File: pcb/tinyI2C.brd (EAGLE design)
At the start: 84 x 83.2 mm, 37 parts, among them IC1 74LVC1G125DCK, IC2 74LVC1G125DCK, IC3 IC_LDO_MIC5355, U1 LPC824M201JHI33, X1 TSW-112-02-S-S, X2 TSW-112-02-S-S, X3 TSW-106-02-S-S-RA, X4 TSW-102-02-S-S, X5 TSW-102-02-S-S, X6 TSW-102-02-S-S

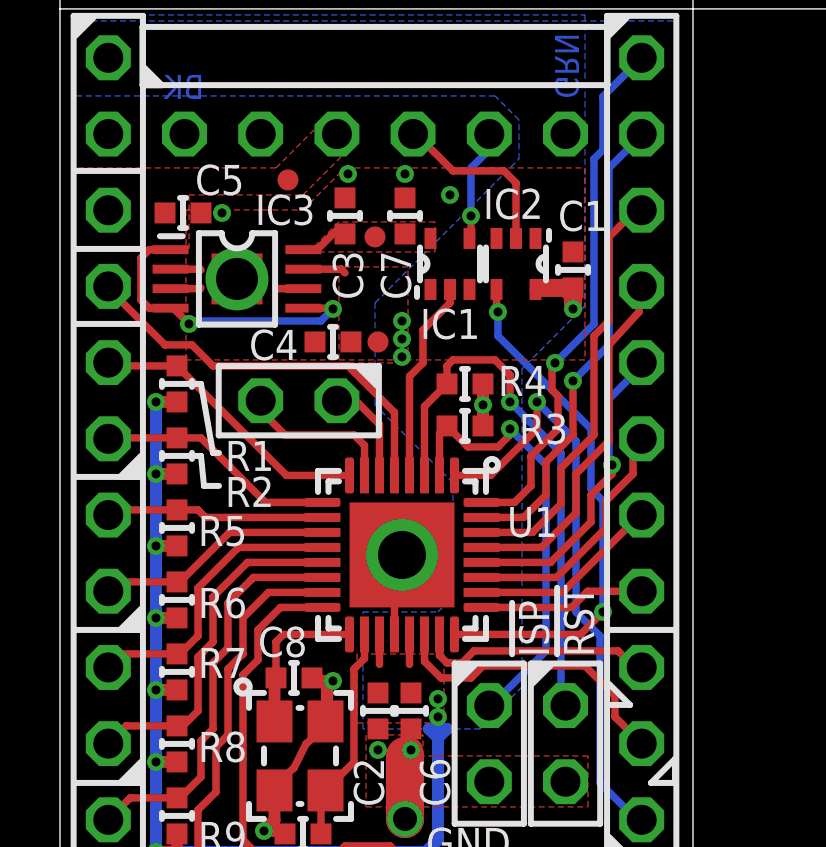
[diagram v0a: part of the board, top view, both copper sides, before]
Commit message: [ PCB ][ BRD ] silk/library update
Silk: pin 1 indicator added (x3)
Library: mylib; IC_LDO_MIC5355; related trace change
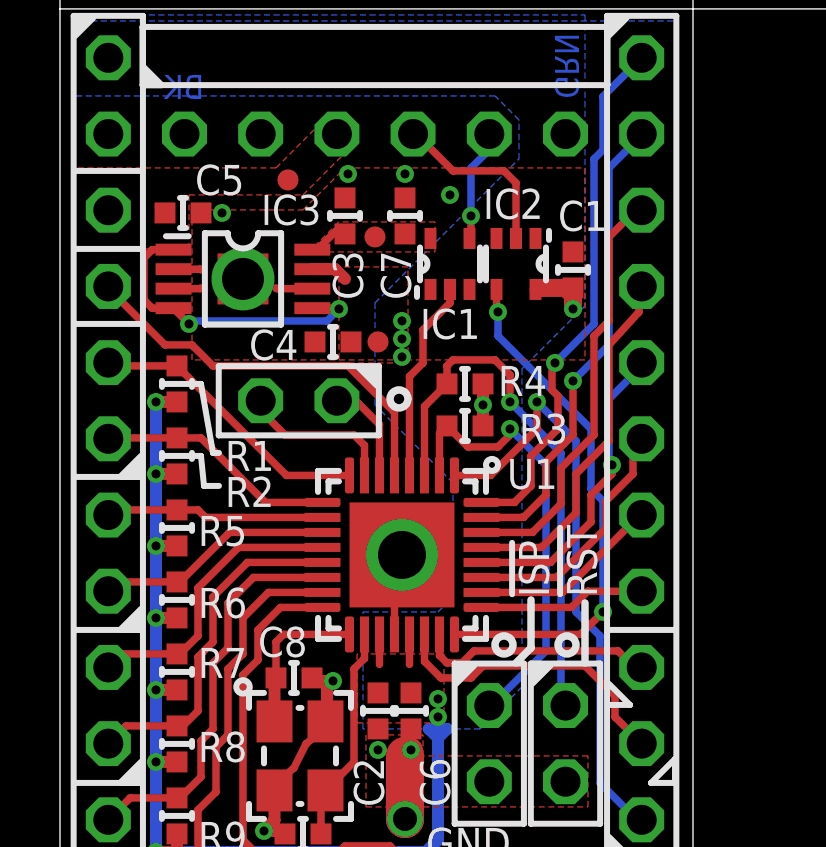
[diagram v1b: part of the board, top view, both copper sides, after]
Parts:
- moved IC3 0.20 mm to (6.10, 32.6)
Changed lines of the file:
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@@
 <grid distance="0.1" unitdist="mm" unit="mm" style="dots" multiple="1" display="yes" altdistance="0.05" altunitdist="mm" altunit="mm"/>
 <layers>
-<layer number="1" name="Top" color="12" fill="1" visible="yes" active="yes"/>
+<layer number="1" name="Top" color="12" fill="0" visible="yes" active="yes"/>
 <layer number="16" name="Bottom" color="1" fill="1" visible="yes" active="yes"/>
 <layer number="17" name="Pads" color="2" fill="1" visible="yes" active="yes"/>
@@
 <wire x1="13.4" y1="32.6" x2="13.4" y2="31.9" width="0.1" layer="41"/>
 <wire x1="13.9" y1="31.9" x2="13.9" y2="32.6" width="0.1" layer="41"/>
-<text x="17.8" y="20" size="1" layer="21" font="vector" ratio="20" rot="R90">!RST</text>
-<text x="16.3" y="20" size="1" layer="21" font="vector" ratio="20" rot="R90">!ISP</text>
+<text x="17.9" y="22" size="1" layer="21" font="vector" ratio="20" rot="R90">!RST</text>
+<text x="16.3" y="22" size="1" layer="21" font="vector" ratio="20" rot="R90">!ISP</text>
 <wire x1="9" y1="30" x2="9" y2="31" width="0.2" layer="41"/>
 <wire x1="9" y1="30" x2="8.2" y2="30" width="0.2" layer="41"/>
@@
 <wire x1="4.7" y1="29.1" x2="5.1" y2="26.8" width="0.2" layer="21"/>
 <wire x1="4.7" y1="26.7" x2="4.8" y2="25.7" width="0.2" layer="21"/>
-<wire x1="11.6" y1="31.7" x2="11.2" y2="31.7" width="0.1" layer="41"/>
-<wire x1="10.6" y1="31.1" x2="11.2" y2="31.7" width="0.1" layer="41" curve="-90"/>
-<wire x1="10.6" y1="33" x2="10.6" y2="31.1" width="0.1" layer="41"/>
+<wire x1="11.6" y1="31.7" x2="11.4" y2="31.7" width="0.1" layer="41"/>
+<wire x1="10.8" y1="31.1" x2="11.4" y2="31.7" width="0.1" layer="41" curve="-90"/>
+<wire x1="10.8" y1="33" x2="10.8" y2="31.1" width="0.1" layer="41"/>
 <wire x1="12.1" y1="31.8" x2="12.1" y2="32.6" width="0.1" layer="41"/>
 <wire x1="12.6" y1="31.8" x2="12.1" y2="31.8" width="0.2" layer="41"/>
@@
 <wire x1="20.5" y1="15.8" x2="20.5" y2="16.6" width="0.2" layer="21"/>
 <wire x1="20.5" y1="16.6" x2="19.7" y2="15.8" width="0.2" layer="21"/>
-<wire x1="7.6" y1="32.5" x2="8.7" y2="32.5" width="0.2" layer="41"/>
-<wire x1="7.6" y1="32" x2="8.7" y2="32" width="0.2" layer="41"/>
-<wire x1="8.7" y1="32" x2="8.7" y2="32.5" width="0.2" layer="41"/>
-<wire x1="4.2" y1="32.5" x2="3.7" y2="32.5" width="0.2" layer="41"/>
-<wire x1="4.2" y1="32" x2="3.7" y2="32" width="0.2" layer="41"/>
+<wire x1="7.9" y1="32.5" x2="9" y2="32.5" width="0.2" layer="41"/>
+<wire x1="7.9" y1="32" x2="9" y2="32" width="0.2" layer="41"/>
+<wire x1="9" y1="32" x2="9" y2="32.5" width="0.2" layer="41"/>
+<wire x1="4.1" y1="32.5" x2="3.6" y2="32.5" width="0.2" layer="41"/>
+<wire x1="4.1" y1="32" x2="3.6" y2="32" width="0.2" layer="41"/>
 <polygon width="0.2" layer="30">
 <vertex x="5.9" y="33.5" curve="-90"/>
@@
 <wire x1="14.2" y1="31.9" x2="13.9" y2="31.9" width="0.1" layer="41"/>
 <wire x1="14.2" y1="32.6" x2="13.9" y2="32.6" width="0.1" layer="41"/>
+<circle x="11.3" y="28.6" radius="0.3" width="0.25" layer="21"/>
+<circle x="14.8" y="20.4" radius="0.3" width="0.25" layer="21"/>
+<circle x="16.9" y="20.4" radius="0.3" width="0.25" layer="21"/>
+<wire x1="15.7" y1="21.9" x2="15.7" y2="20.3" width="0.25" layer="21"/>
+<wire x1="15.7" y1="20.3" x2="15.2" y2="19.8" width="0.25" layer="21"/>
+<wire x1="17.5" y1="21.8" x2="17.5" y2="19.8" width="0.25" layer="21"/>
 </plain>
 <attributes>
@@
 </element>
 <element name="U1" library="mylib" package="HVQFN33" value="LPC824M201JHI33" x="11.4" y="23.4" smashed="yes" rot="R270">
-<attribute name="NAME" x="14.9" y="24" size="1" layer="25" font="vector" ratio="20"/>
+<attribute name="NAME" x="14.9" y="25.6" size="1" layer="25" font="vector" ratio="20"/>
 <attribute name="VALUE" x="6.9" y="25.9" size="1.27" layer="27" ratio="10" rot="R270"/>
 </element>
@@
 <attribute name="VALUE" x="13.405" y="34.065" size="1.27" layer="27" rot="R90"/>
 </element>
-<element name="IC3" library="mylib" package="IC_08_0.65_160MIL" value="IC_LDO_MIC5355" x="5.9" y="32.6" smashed="yes" rot="R270">
-<attribute name="NAME" x="6.5" y="34.4" size="1" layer="25" font="vector" ratio="20"/>
-<attribute name="VALUE" x="3.36" y="29.298" size="1.27" layer="27" ratio="10"/>
+<element name="IC3" library="mylib" package="IC_08_0.65_160MIL" value="IC_LDO_MIC5355" x="6.1" y="32.6" smashed="yes" rot="R270">
+<attribute name="NAME" x="6.7" y="34.4" size="1" layer="25" font="vector" ratio="20"/>
+<attribute name="VALUE" x="3.56" y="29.298" size="1.27" layer="27" ratio="10"/>
 </element>
 <element name="Q1" library="adafruit (1)" package="NX3225" value="" x="8" y="16.7" rot="R270"/>
@@
 <vertex x="0.4" y="10.8"/>
 </polygon>
-<via x="5.9" y="32.6" extent="1-16" drill="1.4" shape="square"/>
+<via x="6.1" y="32.6" extent="1-16" drill="1.4" shape="square"/>
 <contactref element="C3" pad="2"/>
 <contactref element="X1" pad="2"/>
@@
 <contactref element="IC3" pad="EXP"/>
 <contactref element="IC3" pad="2"/>
-<wire x1="3.687" y1="32.926" x2="4.674" y2="32.926" width="0.25" layer="1"/>
+<wire x1="3.787" y1="32.926" x2="4.674" y2="32.926" width="0.25" layer="1"/>
 <wire x1="4.674" y1="32.926" x2="4.7" y2="32.9" width="0.25" layer="1"/>
 <via x="13" y="35.4" extent="1-16" drill="0.3"/>
@@
 <via x="11.5" y="36.1" extent="1-16" drill="0.3"/>
 <polygon width="0.25" layer="1" thermals="no" rank="2">
-<vertex x="4.2" y="34.9"/>
+<vertex x="4.4" y="34.9"/>
 <vertex x="8.1" y="34.9"/>
 <vertex x="9.5" y="36.3"/>
 <vertex x="17.5" y="36.3"/>
 <vertex x="17.5" y="29.9"/>
-<vertex x="4.2" y="29.9"/>
+<vertex x="4.4" y="29.9"/>
 </polygon>
 <wire x1="9.1" y1="19.2" x2="8.9" y2="19" width="0.4" layer="1"/>
@@
 <contactref element="IC3" pad="6"/>
 <contactref element="IC3" pad="3"/>
-<wire x1="3.687" y1="32.276" x2="4.676" y2="32.276" width="0.25" layer="1"/>
+<wire x1="3.787" y1="32.276" x2="4.676" y2="32.276" width="0.25" layer="1"/>
 <wire x1="4.676" y1="32.276" x2="4.7" y2="32.3" width="0.25" layer="1"/>
-<wire x1="8.112" y1="32.276" x2="7.224" y2="32.276" width="0.25" layer="1"/>
+<wire x1="8.412" y1="32.276" x2="7.224" y2="32.276" width="0.25" layer="1"/>
 <wire x1="7.224" y1="32.276" x2="7.2" y2="32.3" width="0.25" layer="1"/>
 <via x="11.5" y="14.6" extent="1-16" drill="0.8"/>
@@
 <contactref element="C5" pad="1"/>
 <contactref element="TP1" pad="TP"/>
-<wire x1="3.687" y1="31.626" x2="2.974" y2="31.626" width="0.25" layer="1"/>
-<wire x1="2.974" y1="31.626" x2="2.7" y2="31.9" width="0.25" layer="1"/>
-<wire x1="3.687" y1="33.576" x2="2.976" y2="33.576" width="0.25" layer="1"/>
-<wire x1="2.976" y1="33.576" x2="2.7" y2="33.3" width="0.25" layer="1"/>
-<wire x1="2.7" y1="33.3" x2="2.7" y2="31.9" width="0.25" layer="1"/>
 <polygon width="0.25" layer="1" thermals="no" rank="3">
 <vertex x="0.5" y="33.6"/>
@@
 <contactref element="X1" pad="3"/>
 <via x="4.3" y="31.1" extent="1-16" drill="0.3"/>
-<via x="9.1" y="31.6" extent="1-16" drill="0.3"/>
+<via x="9.3" y="31.6" extent="1-16" drill="0.3"/>
 <wire x1="4.3" y1="31.1" x2="4.4" y2="31.2" width="0.25" layer="16"/>
-<wire x1="4.4" y1="31.2" x2="8.7" y2="31.2" width="0.25" layer="16"/>
-<wire x1="8.7" y1="31.2" x2="9.1" y2="31.6" width="0.25" layer="16"/>
-<wire x1="8.112" y1="31.626" x2="9.074" y2="31.626" width="0.25" layer="1"/>
-<wire x1="9.074" y1="31.626" x2="9.1" y2="31.6" width="0.25" layer="1"/>
-<wire x1="3.687" y1="31.626" x2="3.774" y2="31.626" width="0.25" layer="1"/>
+<wire x1="4.4" y1="31.2" x2="8.9" y2="31.2" width="0.25" layer="16"/>
+<wire x1="8.9" y1="31.2" x2="9.3" y2="31.6" width="0.25" layer="16"/>
+<wire x1="8.412" y1="31.626" x2="9.274" y2="31.626" width="0.25" layer="1"/>
+<wire x1="9.274" y1="31.626" x2="9.3" y2="31.6" width="0.25" layer="1"/>
+<wire x1="3.787" y1="31.626" x2="3.774" y2="31.626" width="0.25" layer="1"/>
 <wire x1="3.774" y1="31.626" x2="4.3" y2="31.1" width="0.25" layer="1"/>
+<wire x1="3.787" y1="33.576" x2="3.076" y2="33.576" width="0.25" layer="1"/>
+<wire x1="3.076" y1="33.576" x2="2.8" y2="33.3" width="0.25" layer="1"/>
+<wire x1="3.787" y1="31.626" x2="3.074" y2="31.626" width="0.25" layer="1"/>
+<wire x1="3.074" y1="31.626" x2="2.8" y2="31.9" width="0.25" layer="1"/>
+<wire x1="2.8" y1="31.9" x2="2.8" y2="33.3" width="0.25" layer="1"/>
 </signal>
 <signal name="TX-&gt;">
@@
 <wire x1="3.2" y1="13.5" x2="12.2" y2="13.5" width="0.4" layer="16"/>
 <wire x1="12.2" y1="13.5" x2="12.6" y2="13.9" width="0.4" layer="16"/>
-<wire x1="8.112" y1="32.926" x2="9.374" y2="32.926" width="0.25" layer="1"/>
-<wire x1="9.374" y1="32.926" x2="9.5" y2="32.8" width="0.25" layer="1"/>
+<wire x1="8.412" y1="32.926" x2="9.174" y2="32.926" width="0.4" layer="1"/>
+<wire x1="9.174" y1="32.926" x2="9.5" y2="32.6" width="0.4" layer="1"/>
 <contactref element="IC2" pad="5"/>
 <polygon width="0.25" layer="1" thermals="no">
@@
 <contactref element="C3" pad="1"/>
 <contactref element="TP6" pad="TP"/>
-<wire x1="8.112" y1="33.576" x2="8.576" y2="33.576" width="0.25" layer="1"/>
+<wire x1="8.412" y1="33.576" x2="8.576" y2="33.576" width="0.25" layer="1"/>
 <wire x1="8.576" y1="33.576" x2="9.2" y2="34.2" width="0.25" layer="1"/>
 <contactref element="C7" pad="1"/>

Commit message: [ PCB ][ BRD ] IC2/C1 moved; 1.8V line narrowed
IC2: turned 90deg CW
C1: moved to fit
1.8V: narrowed; getting wider GND
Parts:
- moved C1 2.16 mm to (15.9, 34.7), turned to 180 degrees
- moved IC2 0.54 mm to (15.7, 32.9), turned to 270 degrees
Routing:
- net 1.8V: track 42.8 -> 88.2 mm
- net TX->: track 5.96 -> 11.3 mm
